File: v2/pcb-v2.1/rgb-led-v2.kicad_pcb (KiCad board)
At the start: 2 copper layers, 90 x 50 mm, 12 parts, among them CON1 BARREL_JACK, SW1 SPST

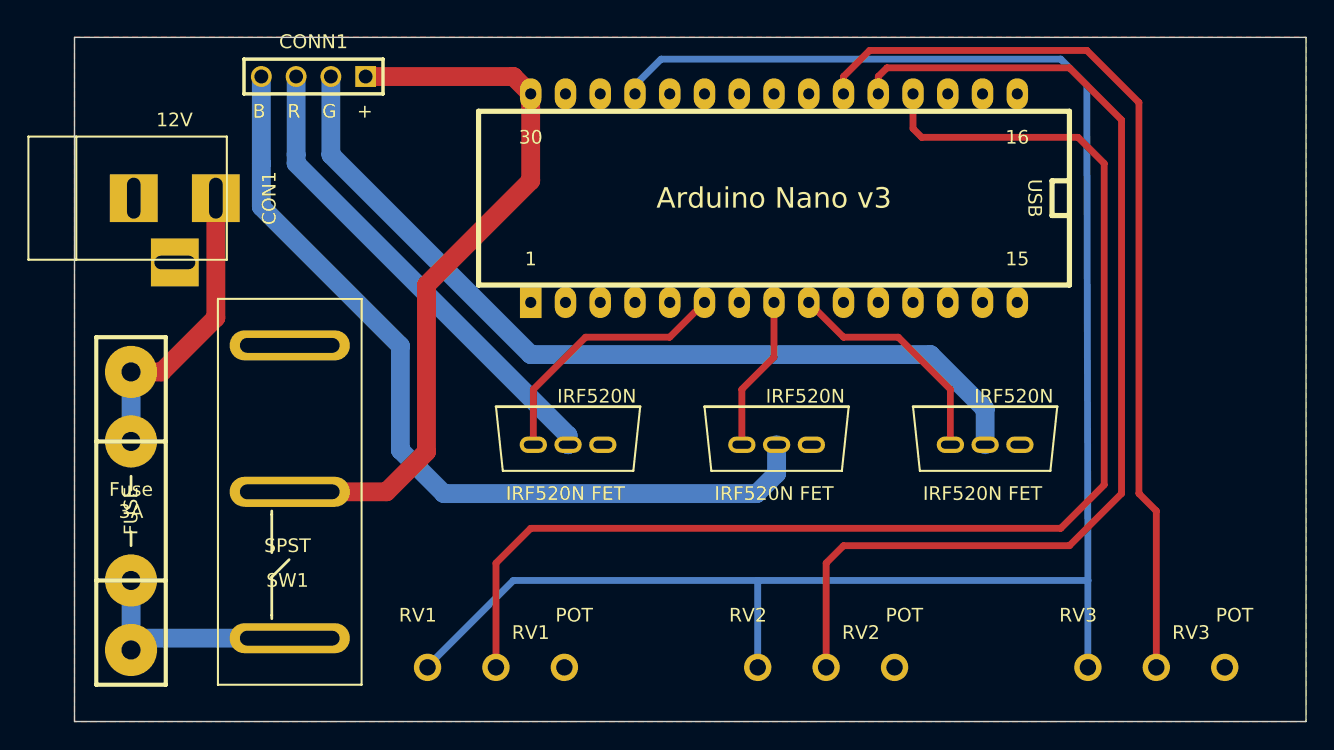
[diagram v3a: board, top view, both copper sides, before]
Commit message: Add mounting holes
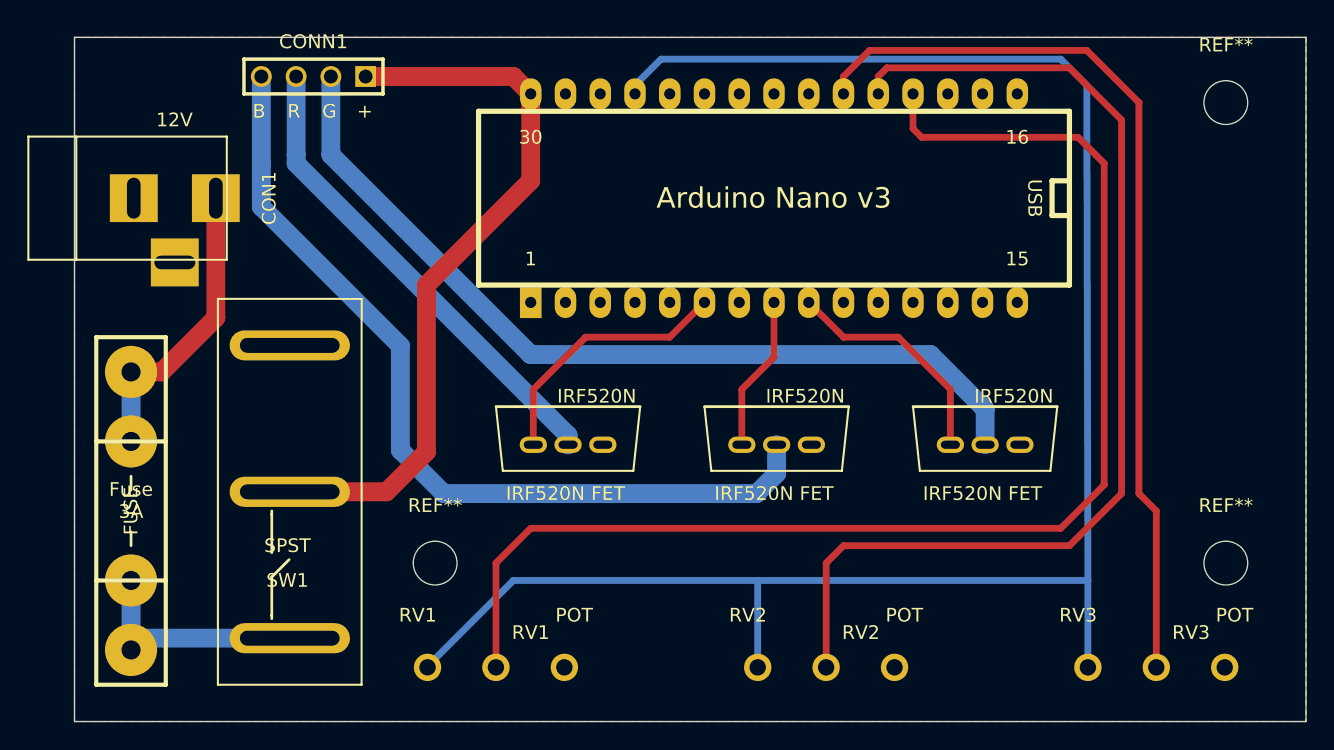
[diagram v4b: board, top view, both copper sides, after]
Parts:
- added REF**: MountingHole_3.2mm_M3, Mounting_Holes:MountingHole_3.2mm_M3, F.Cu at (102.9, 24.8)
- added REF**: MountingHole_3.2mm_M3, Mounting_Holes:MountingHole_3.2mm_M3, F.Cu at (45.1, 58.4)
- added REF**: MountingHole_3.2mm_M3, Mounting_Holes:MountingHole_3.2mm_M3, F.Cu at (102.9, 58.4)
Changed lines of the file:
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@@
     (tracks 83)
     (zones 0)
-    (modules 12)
+    (modules 15)
     (nets 35)
   )
@@
     (42 Eco1.User user)
     (43 Eco2.User user)
-    (44 Edge.Cuts user hide)
+    (44 Edge.Cuts user)
   )
   (setup
@@
       (net 1 GND))
   )
+  (module Mounting_Holes:MountingHole_3.2mm_M3 (layer F.Cu)
+    (at 102.87 24.765)
+    (descr "Mounting Hole 3.2mm, no annular, M3")
+    (tags "mounting hole 3.2mm no annular m3")
+    (fp_text reference REF** (at 0 -4.2) (layer F.SilkS)
+      (effects (font (size 1 1) (thickness 0.15)))
+    )
+    (fp_text value MountingHole_3.2mm_M3 (at 0 4.2) (layer F.Fab)
+      (effects (font (size 1 1) (thickness 0.15)))
+    )
+    (fp_circle (center 0 0) (end 3.2 0) (layer Cmts.User) (width 0.15))
+    (fp_circle (center 0 0) (end 3.45 0) (layer F.CrtYd) (width 0.05))
+    (pad 1 np_thru_hole circle (at 0 0) (size 3.2 3.2) (drill 3.2) (layers *.Cu *.Mask F.SilkS))
+  )
+  (module Mounting_Holes:MountingHole_3.2mm_M3 (layer F.Cu)
+    (at 45.085 58.42)
+    (descr "Mounting Hole 3.2mm, no annular, M3")
+    (tags "mounting hole 3.2mm no annular m3")
+    (fp_text reference REF** (at 0 -4.2) (layer F.SilkS)
+      (effects (font (size 1 1) (thickness 0.15)))
+    )
+    (fp_text value MountingHole_3.2mm_M3 (at 0 4.2) (layer F.Fab)
+      (effects (font (size 1 1) (thickness 0.15)))
+    )
+    (fp_circle (center 0 0) (end 3.2 0) (layer Cmts.User) (width 0.15))
+    (fp_circle (center 0 0) (end 3.45 0) (layer F.CrtYd) (width 0.05))
+    (pad 1 np_thru_hole circle (at 0 0) (size 3.2 3.2) (drill 3.2) (layers *.Cu *.Mask F.SilkS))
+  )
+  (module Mounting_Holes:MountingHole_3.2mm_M3 (layer F.Cu)
+    (at 102.87 58.42)
+    (descr "Mounting Hole 3.2mm, no annular, M3")
+    (tags "mounting hole 3.2mm no annular m3")
+    (fp_text reference REF** (at 0 -4.2) (layer F.SilkS)
+      (effects (font (size 1 1) (thickness 0.15)))
+    )
+    (fp_text value MountingHole_3.2mm_M3 (at 0 4.2) (layer F.Fab)
+      (effects (font (size 1 1) (thickness 0.15)))
+    )
+    (fp_circle (center 0 0) (end 3.2 0) (layer Cmts.User) (width 0.15))
+    (fp_circle (center 0 0) (end 3.45 0) (layer F.CrtYd) (width 0.05))
+    (pad 1 np_thru_hole circle (at 0 0) (size 3.2 3.2) (drill 3.2) (layers *.Cu *.Mask F.SilkS))
+  )
   (gr_text RV3 (at 100.33 63.5) (layer F.SilkS)
     (effects (font (size 1 1) (thickness 0.15)))
@@
     (effects (font (size 1.4 1.4) (thickness 0.25)))
   )
-  (gr_text "coredump\nRGB LED V2.1 2016" (at 104.14 43.18 270) (layer F.Mask)
-    (effects (font (size 2 2) (thickness 0.3)))
+  (gr_text "coredump\nRGB LED V2.1 2016" (at 102.87 41.91 270) (layer F.Mask)
+    (effects (font (size 1.7 1.7) (thickness 0.3)))
   )
   (gr_line (start 18.73 20) (end 18.73 70) (angle 90) (layer Edge.Cuts) (width 0.1))
